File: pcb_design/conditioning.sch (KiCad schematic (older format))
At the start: 41 parts, among them U3 OPA2376AID, U4 LM2903-SO8

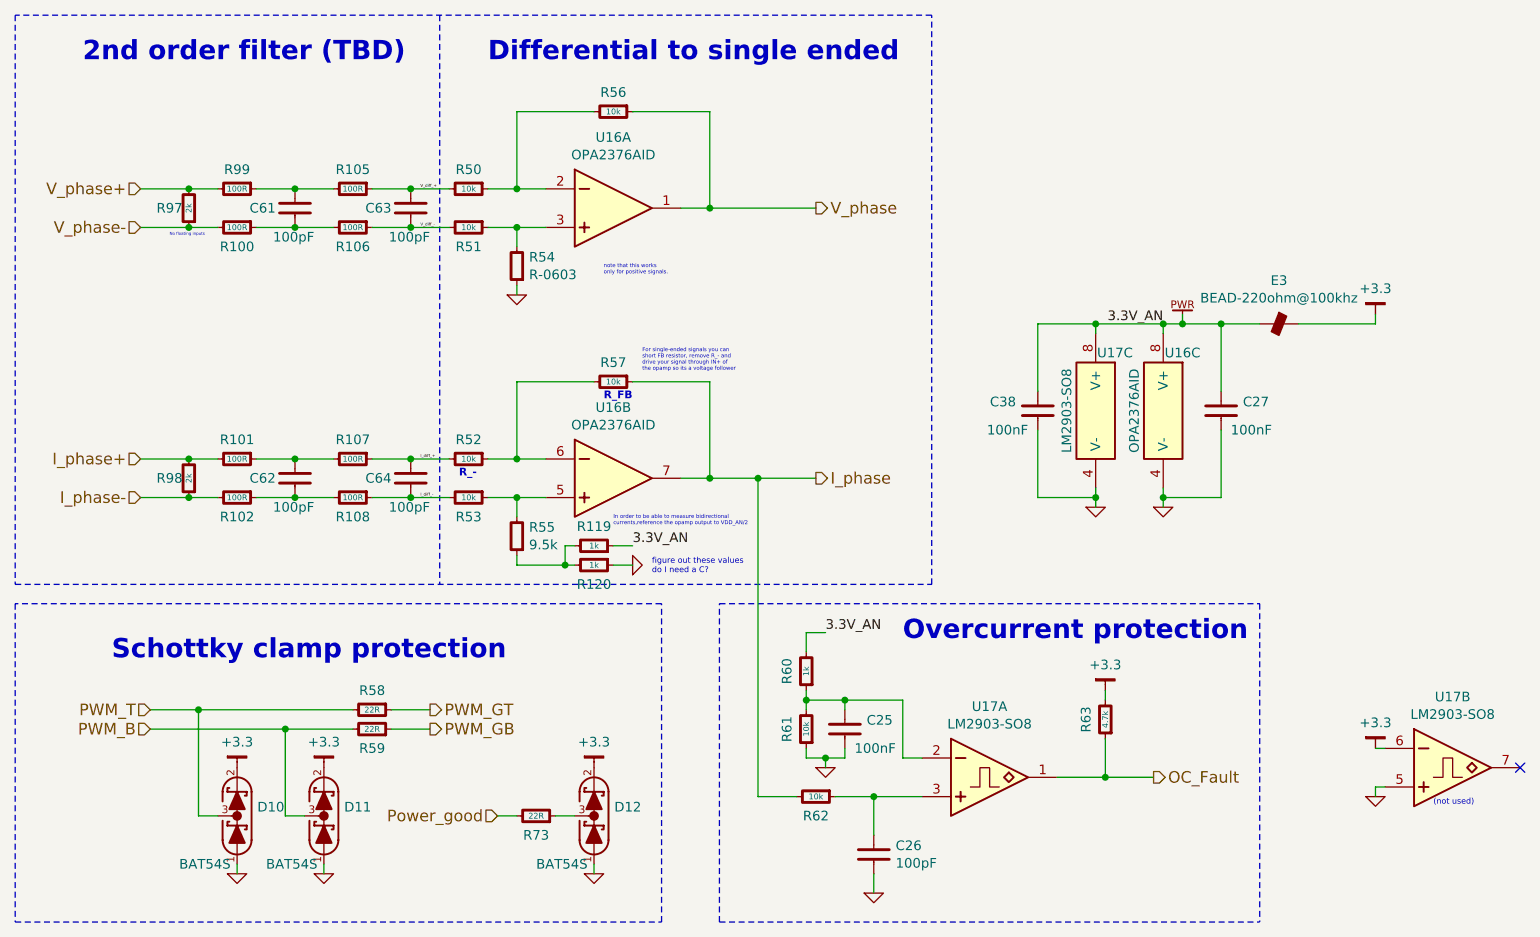
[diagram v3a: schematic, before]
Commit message: Silkscreen logos, fixed swapped OCP inputs, added a button to enter bootloader,missing 3d model.
Signed-off-by: Marcos Chaparro <mchaparro@paltatech.com>
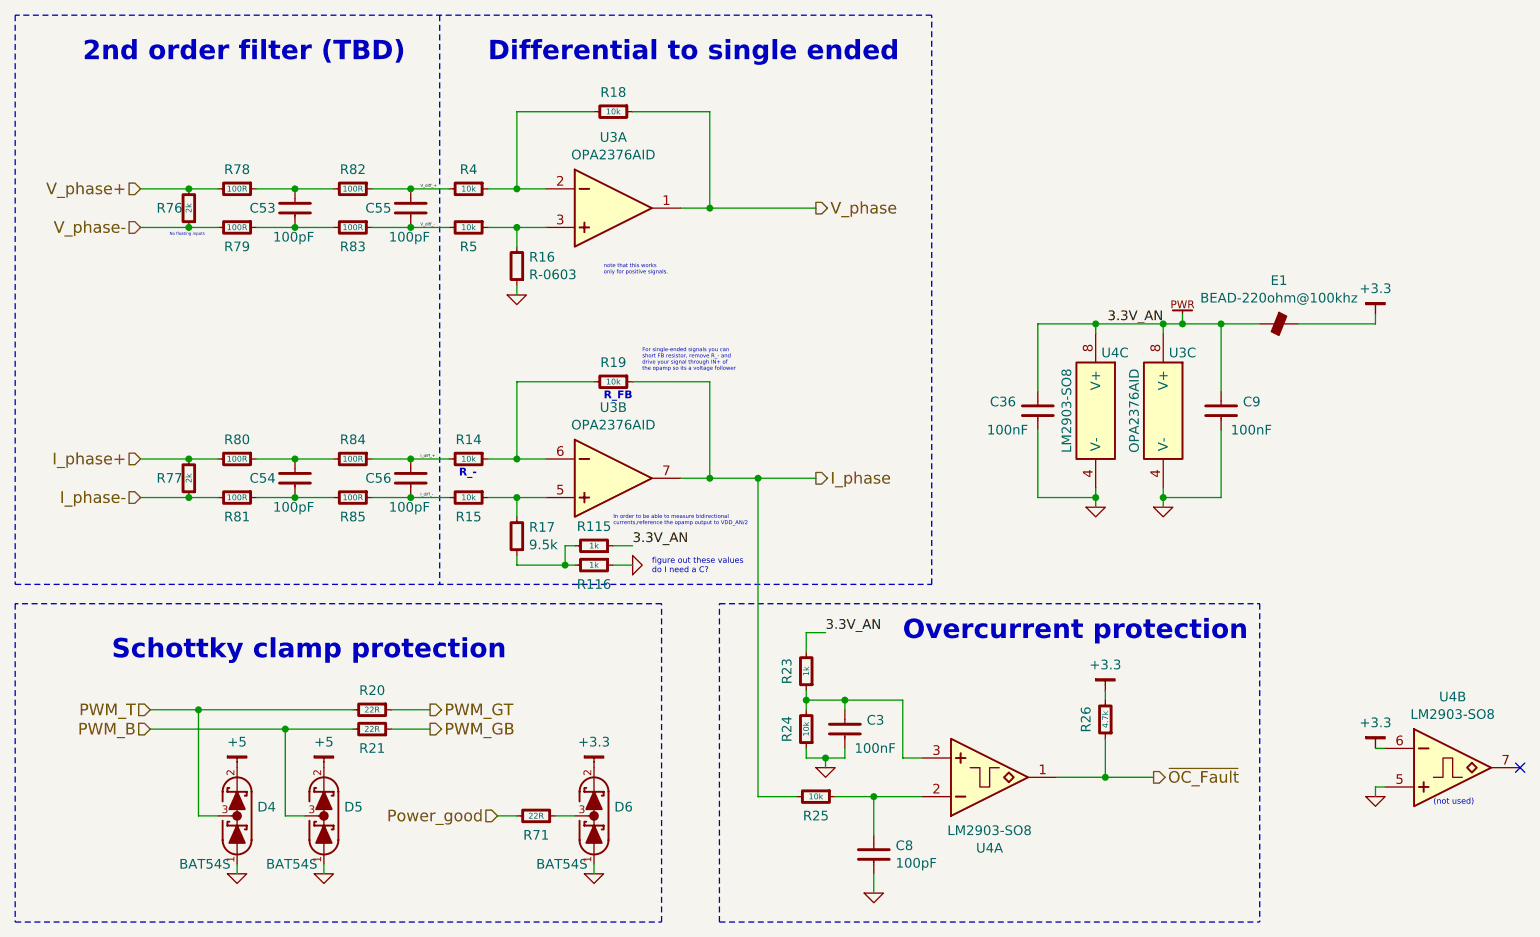
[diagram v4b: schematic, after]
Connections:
- net +3.3: no longer D4.2 (K), D5.2 (K)
- net at C8.1, R25.1: now also U4.2 (IN-); no longer U4.3 (IN+)
- net at C3.1, R23.1, R24.2: now also U4.3 (IN+); no longer U4.2 (IN-)
- net OC_Fault renamed ~OC_Fault
- new net +5: D4.2 (K), D5.2 (K)

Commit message: Updated component values according to simulations. 1.5khz for user inputs and  240khz lp pass filters for motor control
Signed-off-by: Marcos Chaparro <mchaparro@paltatech.com>
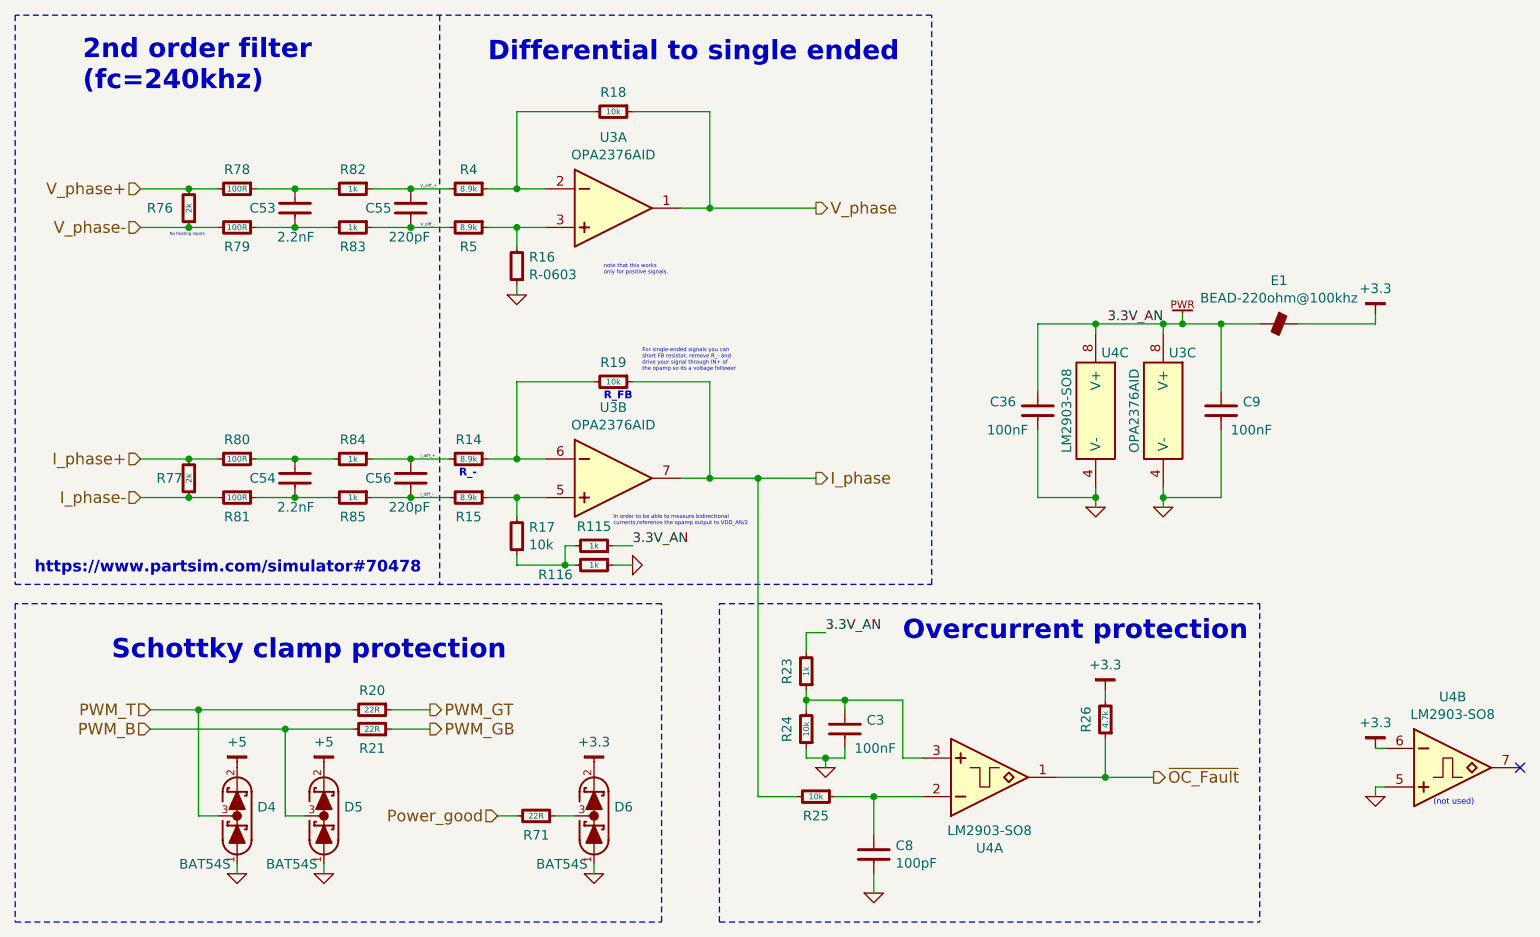
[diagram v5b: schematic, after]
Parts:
- C53, C54: value 100pF -> 2.2nF
- C55, C56: value 100pF -> 220pF
- D4, D5, D6: mfg# (none) -> TBAT54S,LM
- R14, R15, R4, R5: value 10k -> 8.9k
- R17: value 9.5k -> 10k
- R20, R21, R71: mfg# (none) -> RC0603FR-0722RL
- R82, R83, R84, R85: value 100R -> 1k
- U3: mfg# (none) -> OPA2376AIDR
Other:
- note added: "2nd order filter\n(fc=240khz)"
- note added: "https://www.partsim.com/simulator#70478"
- note removed: "2nd order filter (TBD)"
- note removed: "figure out these values\ndo I need a C?"
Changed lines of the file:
@@
 F 2 "IPC7351-Nominal:SOIC127P600X175-8" H 5550 2300 50  0001 C CNN
 F 3 "" V 5550 2700 60  0000 C CNN
-F 4 "IC TI OPA2376AID" H 5550 2200 60  0001 C CNN "BOM"
+F 4 "OPA2376AIDR" H 5550 2550 60  0001 C CNN "mfg#"
+F 5 "IC TI OPA2376AID" H 5550 2200 60  0001 C CNN "BOM"
 	1    5550 2550
 	1    0    0    -1
@@
 AR Path="/588C4E84/588D8E6C" Ref="R50"  Part="1"
 F 0 "R4" V 4750 2450 50  0000 C CNN
-F 1 "10k" V 4850 2450 30  0000 C CNN
+F 1 "8.9k" V 4850 2450 30  0000 C CNN
 F 2 "IPC7351-Nominal:RESC1608X50" H 4850 2450 50  0001 C CNN
 F 3 "" H 4850 2500 60  0000 C CNN
@@
 AR Path="/588C4E84/588D8EA7" Ref="R51"  Part="1"
 F 0 "R5" V 4950 2650 50  0000 C CNN
-F 1 "10k" V 4850 2650 30  0000 C CNN
+F 1 "8.9k" V 4850 2650 30  0000 C CNN
 F 2 "IPC7351-Nominal:RESC1608X50" H 4850 2650 50  0001 C CNN
 F 3 "" H 4850 2700 60  0000 C CNN
@@
 F 2 "IPC7351-Nominal:SOIC127P600X175-8" H 5550 3700 50  0001 C CNN
 F 3 "" V 5550 4100 60  0000 C CNN
-F 4 "IC TI OPA2376AID" H 5550 3600 60  0001 C CNN "BOM"
+F 4 "OPA2376AIDR" H 5550 3950 60  0001 C CNN "mfg#"
+F 5 "IC TI OPA2376AID" H 5550 3600 60  0001 C CNN "BOM"
 	2    5550 3950
 	1    0    0    -1
@@
 AR Path="/588C4E84/588D96DC" Ref="R52"  Part="1"
 F 0 "R14" V 4750 3850 50  0000 C CNN
-F 1 "10k" V 4850 3850 30  0000 C CNN
+F 1 "8.9k" V 4850 3850 30  0000 C CNN
 F 2 "IPC7351-Nominal:RESC1608X50" H 4850 3850 50  0001 C CNN
 F 3 "" H 4850 3900 60  0000 C CNN
@@
 AR Path="/588C4E84/588D96E3" Ref="R53"  Part="1"
 F 0 "R15" V 4950 4050 50  0000 C CNN
-F 1 "10k" V 4850 4050 30  0000 C CNN
+F 1 "8.9k" V 4850 4050 30  0000 C CNN
 F 2 "IPC7351-Nominal:RESC1608X50" H 4850 4050 50  0001 C CNN
 F 3 "" H 4850 4100 60  0000 C CNN
@@
 AR Path="/588C4E84/588D96F1" Ref="R55"  Part="1"
 F 0 "R17" H 5037 4204 50  0000 R CNN
-F 1 "9.5k" H 5037 4295 50  0000 R CNN
+F 1 "10k" H 5037 4295 50  0000 R CNN
 F 2 "IPC7351-Nominal:RESC1608X50" H 5100 4250 50  0001 C CNN
 F 3 "" H 5100 4300 60  0000 C CNN
@@
 F 2 "IPC7351-Nominal:SOIC127P600X175-8" H 8450 3350 50  0001 C CNN
 F 3 "" V 8450 3750 60  0000 C CNN
-F 4 "IC TI OPA2376AID" H 8450 3250 60  0001 C CNN "BOM"
+F 4 "OPA2376AIDR" H 8450 3600 60  0001 C CNN "mfg#"
+F 5 "IC TI OPA2376AID" H 8450 3250 60  0001 C CNN "BOM"
 	3    8450 3600
 	1    0    0    -1
@@
 F 2 "smd-semi:SOT-23" H 3650 5550 60  0001 C CNN
 F 3 "" V 3600 5700 60  0000 C CNN
-F 4 "SCHOTTKY BAT54S" H 3650 5450 60  0001 C CNN "BOM"
+F 4 "TBAT54S,LM" H 3650 5700 60  0001 C CNN "mfg#"
+F 5 "SCHOTTKY BAT54S" H 3650 5450 60  0001 C CNN "BOM"
 	1    3650 5700
 	0    -1   -1   0
@@
 F 2 "smd-semi:SOT-23" H 4100 5550 60  0001 C CNN
 F 3 "" V 4050 5700 60  0000 C CNN
-F 4 "SCHOTTKY BAT54S" H 4100 5450 60  0001 C CNN "BOM"
+F 4 "TBAT54S,LM" H 4100 5700 60  0001 C CNN "mfg#"
+F 5 "SCHOTTKY BAT54S" H 4100 5450 60  0001 C CNN "BOM"
 	1    4100 5700
 	0    -1   -1   0
@@
 F 2 "smd-semi:SOT-23" H 5500 5550 60  0001 C CNN
 F 3 "" V 5450 5700 60  0000 C CNN
-F 4 "SCHOTTKY BAT54S" H 5500 5450 60  0001 C CNN "BOM"
+F 4 "TBAT54S,LM" H 5500 5700 60  0001 C CNN "mfg#"
+F 5 "SCHOTTKY BAT54S" H 5500 5450 60  0001 C CNN "BOM"
 	1    5500 5700
 	0    -1   -1   0
@@
 F 2 "IPC7351-Nominal:RESC1608X50" H 4350 5150 50  0001 C CNN
 F 3 "" H 4350 5200 60  0000 C CNN
-F 4 "RES SMD 1k 5% [0603]" H 5100 5700 60  0001 C CNN "BOM"
+F 4 "RC0603FR-0722RL" H 4350 5150 60  0001 C CNN "mfg#"
+F 5 "RES SMD 1k 5% [0603]" H 5100 5700 60  0001 C CNN "BOM"
 	1    4350 5150
 	0    1    1    0
@@
 F 2 "IPC7351-Nominal:RESC1608X50" H 4350 5250 50  0001 C CNN
 F 3 "" H 4350 5300 60  0000 C CNN
-F 4 "RES SMD 1k 5% [0603]" H 5100 5800 60  0001 C CNN "BOM"
+F 4 "RC0603FR-0722RL" H 4350 5250 60  0001 C CNN "mfg#"
+F 5 "RES SMD 1k 5% [0603]" H 5100 5800 60  0001 C CNN "BOM"
 	1    4350 5250
 	0    1    -1   0
@@
 F 2 "IPC7351-Nominal:RESC1608X50" H 5200 5700 50  0001 C CNN
 F 3 "" H 5200 5750 60  0000 C CNN
-F 4 "RES SMD 1k 5% [0603]" H 5950 6250 60  0001 C CNN "BOM"
+F 4 "RC0603FR-0722RL" H 5200 5700 60  0001 C CNN "mfg#"
+F 5 "RES SMD 1k 5% [0603]" H 5950 6250 60  0001 C CNN "BOM"
 	1    5200 5700
 	0    1    -1   0
@@
 AR Path="/588C4E84/588AB1F3" Ref="C63"  Part="1"
 F 0 "C55" H 4650 2550 50  0000 L CNN
-F 1 "100pF" H 4450 2400 50  0000 L CNN
+F 1 "220pF" H 4450 2400 50  0000 L CNN
 F 2 "IPC7351-Nominal:CAPC1608X55" H 4550 2550 50  0001 C CNN
 F 3 "" H 4540 2525 60  0000 C CNN
@@
 AR Path="/588C4E84/588AB6F5" Ref="R105"  Part="1"
 F 0 "R82" V 4150 2450 50  0000 C CNN
-F 1 "100R" V 4250 2450 30  0000 C CNN
+F 1 "1k" V 4250 2450 30  0000 C CNN
 F 2 "IPC7351-Nominal:RESC1608X50" H 4250 2450 50  0001 C CNN
 F 3 "" H 4250 2500 60  0000 C CNN
@@
 AR Path="/588C4E84/588AB79B" Ref="R106"  Part="1"
 F 0 "R83" V 4350 2650 50  0000 C CNN
-F 1 "100R" V 4250 2650 30  0000 C CNN
+F 1 "1k" V 4250 2650 30  0000 C CNN
 F 2 "IPC7351-Nominal:RESC1608X50" H 4250 2650 50  0001 C CNN
 F 3 "" H 4250 2700 60  0000 C CNN
@@
 AR Path="/588C4E84/588ADA39" Ref="C61"  Part="1"
 F 0 "C53" H 4050 2550 50  0000 L CNN
-F 1 "100pF" H 3850 2400 50  0000 L CNN
+F 1 "2.2nF" H 3850 2400 50  0000 L CNN
 F 2 "IPC7351-Nominal:CAPC1608X55" H 3950 2550 50  0001 C CNN
 F 3 "" H 3940 2525 60  0000 C CNN
@@
 AR Path="/588C4E84/588AE424" Ref="C64"  Part="1"
 F 0 "C56" H 4650 3950 50  0000 L CNN
-F 1 "100pF" H 4450 3800 50  0000 L CNN
+F 1 "220pF" H 4450 3800 50  0000 L CNN
 F 2 "IPC7351-Nominal:CAPC1608X55" H 4550 3950 50  0001 C CNN
 F 3 "" H 4540 3925 60  0000 C CNN
@@
 AR Path="/588C4E84/588AE42B" Ref="R107"  Part="1"
 F 0 "R84" V 4150 3850 50  0000 C CNN
-F 1 "100R" V 4250 3850 30  0000 C CNN
+F 1 "1k" V 4250 3850 30  0000 C CNN
 F 2 "IPC7351-Nominal:RESC1608X50" H 4250 3850 50  0001 C CNN
 F 3 "" H 4250 3900 60  0000 C CNN
@@
 AR Path="/588C4E84/588AE432" Ref="R108"  Part="1"
 F 0 "R85" V 4350 4050 50  0000 C CNN
-F 1 "100R" V 4250 4050 30  0000 C CNN
+F 1 "1k" V 4250 4050 30  0000 C CNN
 F 2 "IPC7351-Nominal:RESC1608X50" H 4250 4050 50  0001 C CNN
 F 3 "" H 4250 4100 60  0000 C CNN
@@
 AR Path="/588C4E84/588AE43D" Ref="C62"  Part="1"
 F 0 "C54" H 4050 3950 50  0000 L CNN
-F 1 "100pF" H 3850 3800 50  0000 L CNN
+F 1 "2.2nF" H 3850 3800 50  0000 L CNN
 F 2 "IPC7351-Nominal:CAPC1608X55" H 3950 3950 50  0001 C CNN
 F 3 "" H 3940 3925 60  0000 C CNN
@@
 	0    1    1    0
 $EndComp
-Text Notes 2850 1800 0    100  ~ 20
-2nd order filter (TBD)
+Text Notes 2850 1950 0    100  ~ 20
+2nd order filter\n(fc=240khz)
 $Comp
 L +3.3 #PWR74
@@
 AR Path="/588C2790/588C3F4E" Ref="R87"  Part="1"
 AR Path="/588C4E84/588C3F4E" Ref="R97"  Part="1"
-F 0 "R76" H 3500 2550 50  0000 C CNN
+F 0 "R76" H 3550 2550 50  0000 C CNN
 F 1 "2k" V 3400 2550 30  0000 C CNN
 F 2 "IPC7351-Nominal:RESC1608X50" H 3400 2550 50  0001 C CNN
@@
 AR Path="/588C2790/588D9040" Ref="R118"  Part="1"
 AR Path="/588C4E84/588D9040" Ref="R120"  Part="1"
-F 0 "R116" V 5600 4400 50  0000 C CNN
+F 0 "R116" V 5550 4200 50  0000 C CNN
 F 1 "1k" V 5500 4400 30  0000 C CNN
 F 2 "IPC7351-Nominal:RESC1608X50" H 5500 4400 50  0001 C CNN
@@
 	0    1    -1   0
 $EndComp
-Text Notes 5800 4450 0    30   ~ 0
-figure out these values\ndo I need a C?
 Text Notes 5600 4200 0    20   ~ 0
 In order to be able to measure bidirectional\ncurrents,reference the opamp output to VDD_AN/2
@@
 	1    0    0    -1
 $EndComp
+Text Notes 2600 4450 0    60   ~ 12
+https://www.partsim.com/simulator#70478
 $EndSCHEMATC

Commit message: Completed some part numbers
Signed-off-by: Marcos Chaparro <mchaparro@paltatech.com>
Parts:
- C3, C36, C9: MFR (none) -> Murata Electronics North America; MPN (none) -> GRM188R71E104KA01D; SPN (none) -> 490-1524-1-ND; SPR (none) -> Digikey
- C53, C54: MFR (none) -> Murata Electronics North America; MPN (none) -> GRM188R71H222KA01D; SPN (none) -> 490-1500-1-ND; SPR (none) -> Digikey
- C55, C56: MFR (none) -> Murata Electronics North America; MPN (none) -> GRM1885C1H221JA01D; SPN (none) -> 490-1435-1-ND; SPR (none) -> Digikey
- C8: MFR (none) -> KEMET; MPN (none) -> C0603C101J5GACTU; SPN (none) -> 399-1061-1-ND; SPR (none) -> Digikey
